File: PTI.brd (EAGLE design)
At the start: 65 x 30 mm, 48 parts, among them J1 GPIO, J2 Micro USB, J3 Micro USB, T1 MMUN2133LT1G, U1 MCP73871, U2 TPS61090RSAR, U3 MAX1704X

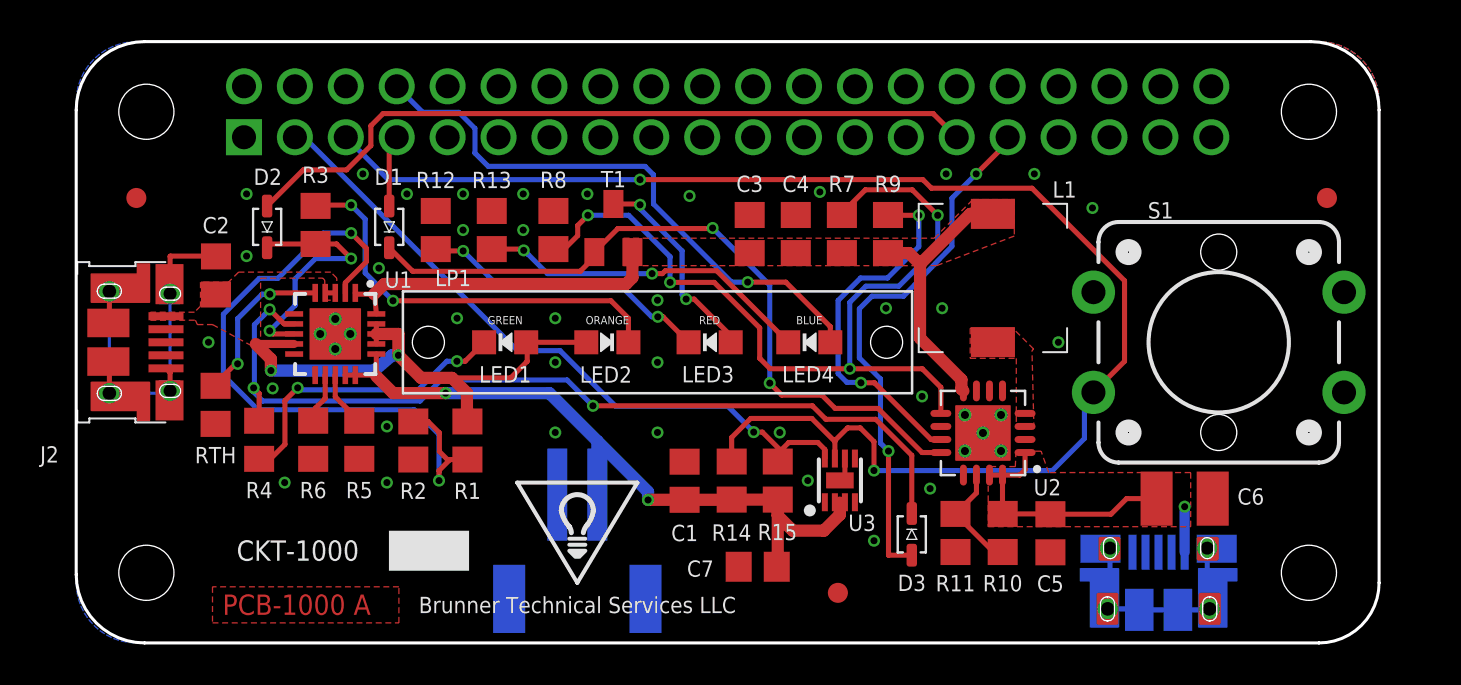
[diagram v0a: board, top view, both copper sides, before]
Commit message: Rev B adds 2mm to the left side of the board to facilitate USB connections.
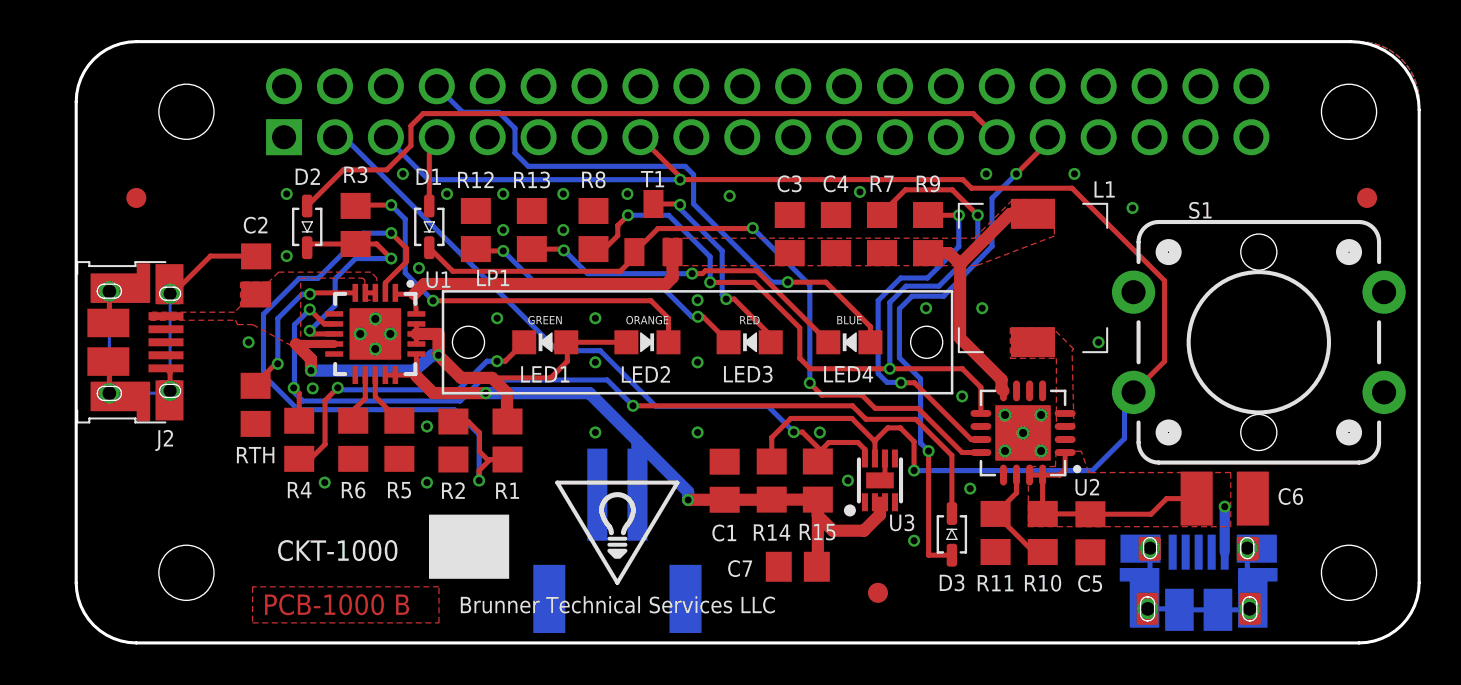
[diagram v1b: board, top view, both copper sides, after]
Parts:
- moved FID1 2.00 mm to (64.4, 22.2)
- moved C2 2.00 mm to (8.97, 18.3)
- moved B1 2.00 mm to (27.0, 3.70)
- moved C1 2.00 mm to (32.4, 8.09)
- moved C3 2.00 mm to (35.6, 20.4)
- moved C4 2.00 mm to (37.9, 20.4)
- moved C5 2.00 mm to (50.6, 5.47)
- moved C6 2.00 mm to (57.3, 7.20)
- moved C7 2.00 mm to (36.0, 3.80)
- moved D2 2.00 mm to (11.5, 20.8)
- moved D3 2.00 mm to (43.7, 5.42)
- moved FID3 2.00 mm to (40.0, 2.50)
- moved J1 2.00 mm to (34.5, 26.5)
- moved J3 2.00 mm to (56.0, 1.70)
- moved L1 2.00 mm to (47.7, 18.2)
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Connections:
- net SCL: now also J1.P$15
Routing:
- net SCL: track 73.7 -> 76.7 mm
- net GND: track 34.1 -> 35.0 mm
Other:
- board size 65 x 30 mm -> 67 x 30 mm
- board text added: "PCB-1000 B"
- board text removed: "PCB-1000 A"

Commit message: Routes GPIO13 (pin 33 on J1) to the ID pin on J3 (power out to USB manifold).  This GPIO can be used to toggle on/off a MOSFET on the USB manifold used to enable or disable receiver 5V power bus.
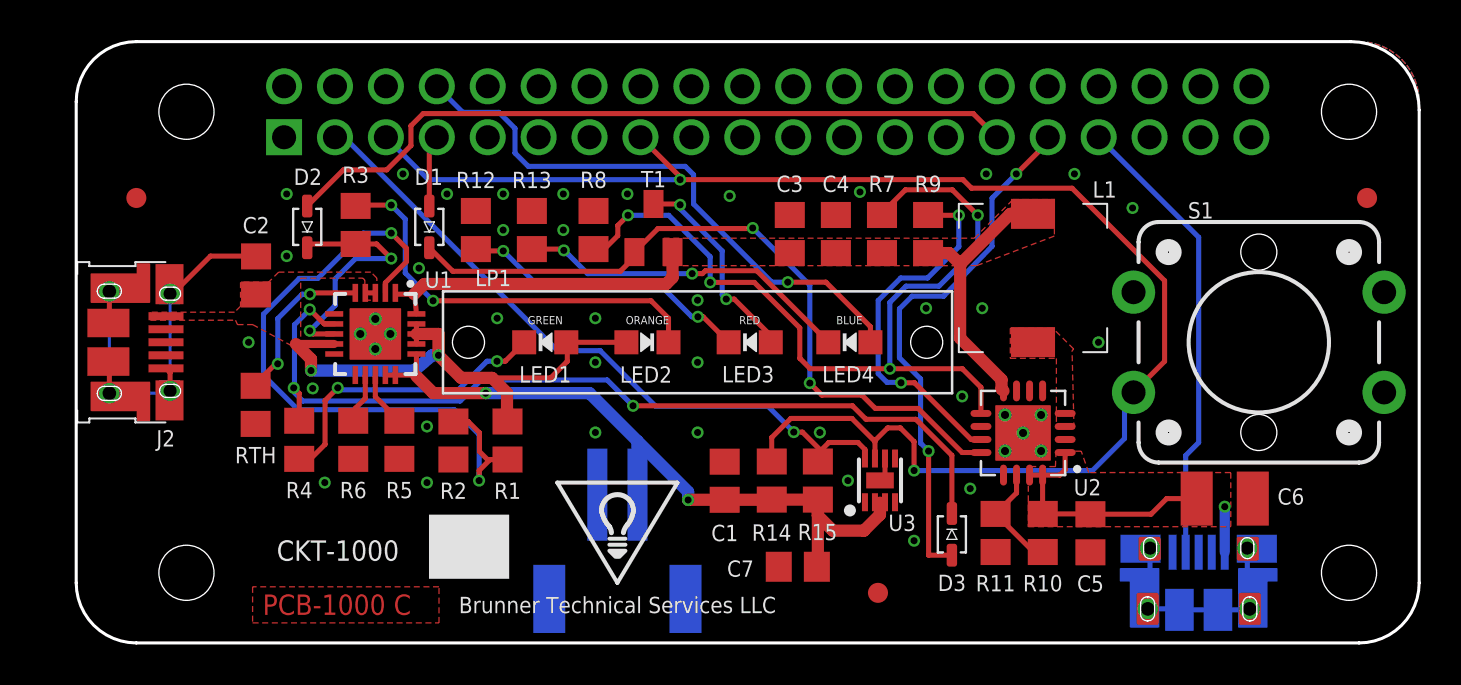
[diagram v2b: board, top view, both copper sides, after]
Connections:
- new net RX_EN: J1.P$33, J3.ID
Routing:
- net RX_EN: track 0.00 -> 23.0 mm
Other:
- board text added: "PCB-1000 C"
- board text removed: "PCB-1000 B"
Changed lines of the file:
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@@
 <?xml version="1.0" encoding="utf-8"?>
 <!DOCTYPE eagle SYSTEM "eagle.dtd">
-<eagle version="9.4.2">
+<eagle version="9.5.1">
 <drawing>
 <settings>
@@
 <layer number="27" name="tValues" color="58" fill="1" visible="yes" active="yes"/>
 <layer number="28" name="bValues" color="58" fill="1" visible="yes" active="yes"/>
-<layer number="29" name="tStop" color="58" fill="3" visible="yes" active="yes"/>
-<layer number="30" name="bStop" color="58" fill="6" visible="yes" active="yes"/>
-<layer number="31" name="tCream" color="58" fill="4" visible="yes" active="yes"/>
-<layer number="32" name="bCream" color="7" fill="5" visible="yes" active="yes"/>
+<layer number="29" name="tStop" color="58" fill="3" visible="no" active="yes"/>
+<layer number="30" name="bStop" color="58" fill="6" visible="no" active="yes"/>
+<layer number="31" name="tCream" color="58" fill="4" visible="no" active="yes"/>
+<layer number="32" name="bCream" color="7" fill="5" visible="no" active="yes"/>
 <layer number="33" name="tFinish" color="6" fill="3" visible="no" active="yes"/>
 <layer number="34" name="bFinish" color="6" fill="6" visible="no" active="yes"/>
-<layer number="35" name="tGlue" color="58" fill="4" visible="yes" active="yes"/>
+<layer number="35" name="tGlue" color="58" fill="4" visible="no" active="yes"/>
 <layer number="36" name="bGlue" color="7" fill="5" visible="no" active="yes"/>
 <layer number="37" name="tTest" color="58" fill="1" visible="no" active="yes"/>
 <layer number="38" name="bTest" color="58" fill="1" visible="no" active="yes"/>
-<layer number="39" name="tKeepout" color="4" fill="11" visible="yes" active="yes"/>
-<layer number="40" name="bKeepout" color="1" fill="11" visible="yes" active="yes"/>
-<layer number="41" name="tRestrict" color="4" fill="10" visible="yes" active="yes"/>
-<layer number="42" name="bRestrict" color="1" fill="10" visible="yes" active="yes"/>
+<layer number="39" name="tKeepout" color="4" fill="11" visible="no" active="yes"/>
+<layer number="40" name="bKeepout" color="1" fill="11" visible="no" active="yes"/>
+<layer number="41" name="tRestrict" color="4" fill="10" visible="no" active="yes"/>
+<layer number="42" name="bRestrict" color="1" fill="10" visible="no" active="yes"/>
 <layer number="43" name="vRestrict" color="2" fill="10" visible="yes" active="yes"/>
-<layer number="44" name="Drills" color="58" fill="1" visible="yes" active="yes"/>
-<layer number="45" name="Holes" color="58" fill="1" visible="yes" active="yes"/>
+<layer number="44" name="Drills" color="58" fill="1" visible="no" active="yes"/>
+<layer number="45" name="Holes" color="58" fill="1" visible="no" active="yes"/>
 <layer number="46" name="Milling" color="3" fill="1" visible="no" active="yes"/>
 <layer number="47" name="Measures" color="58" fill="1" visible="yes" active="yes"/>
@@
 <wire x1="30" y1="8" x2="27" y2="3" width="0.2" layer="21"/>
 <text x="27" y="2.3" size="0.8128" layer="21" ratio="18" align="top-center">Brunner Technical Services LLC</text>
-<text x="9.3" y="1.4" size="1.016" layer="1" ratio="18">PCB-1000 B</text>
+<text x="9.3" y="1.4" size="1.016" layer="1" ratio="18">PCB-1000 C</text>
 <text x="10" y="4.1" size="1.016" layer="21" ratio="12">CKT-1000</text>
 <rectangle x1="17.6" y1="3.2" x2="21.6" y2="6.4" layer="21"/>
@@
 <wire x1="13.328" y1="23.6" x2="15.487925" y2="23.6" width="0.254" layer="1"/>
 </signal>
+<signal name="RX_EN">
+<contactref element="J3" pad="ID"/>
+<contactref element="J1" pad="P$33"/>
+<wire x1="51.01" y1="25.23" x2="56" y2="20.24" width="0.254" layer="16"/>
+<wire x1="56" y1="10" x2="56" y2="20.24" width="0.254" layer="16"/>
+<wire x1="55.35" y1="4.525" x2="55.35" y2="9.35" width="0.254" layer="16"/>
+<wire x1="55.35" y1="9.35" x2="56" y2="10" width="0.254" layer="16"/>
+</signal>
 </signals>
